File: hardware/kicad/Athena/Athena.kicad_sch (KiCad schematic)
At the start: 0 parts

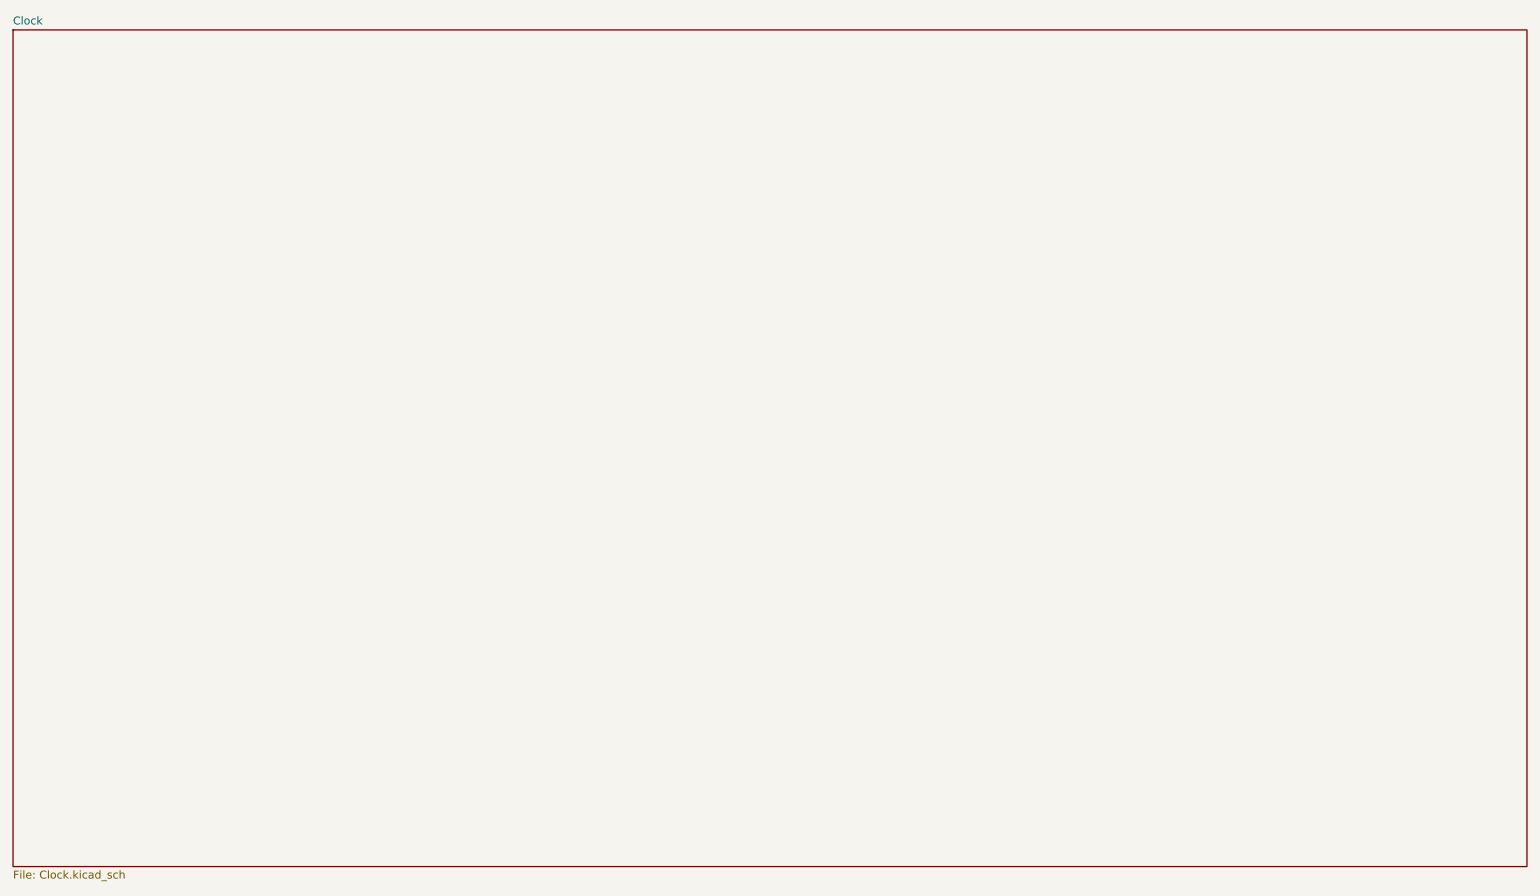
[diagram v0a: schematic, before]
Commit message: Document clock verification and initial Z80 bring-up
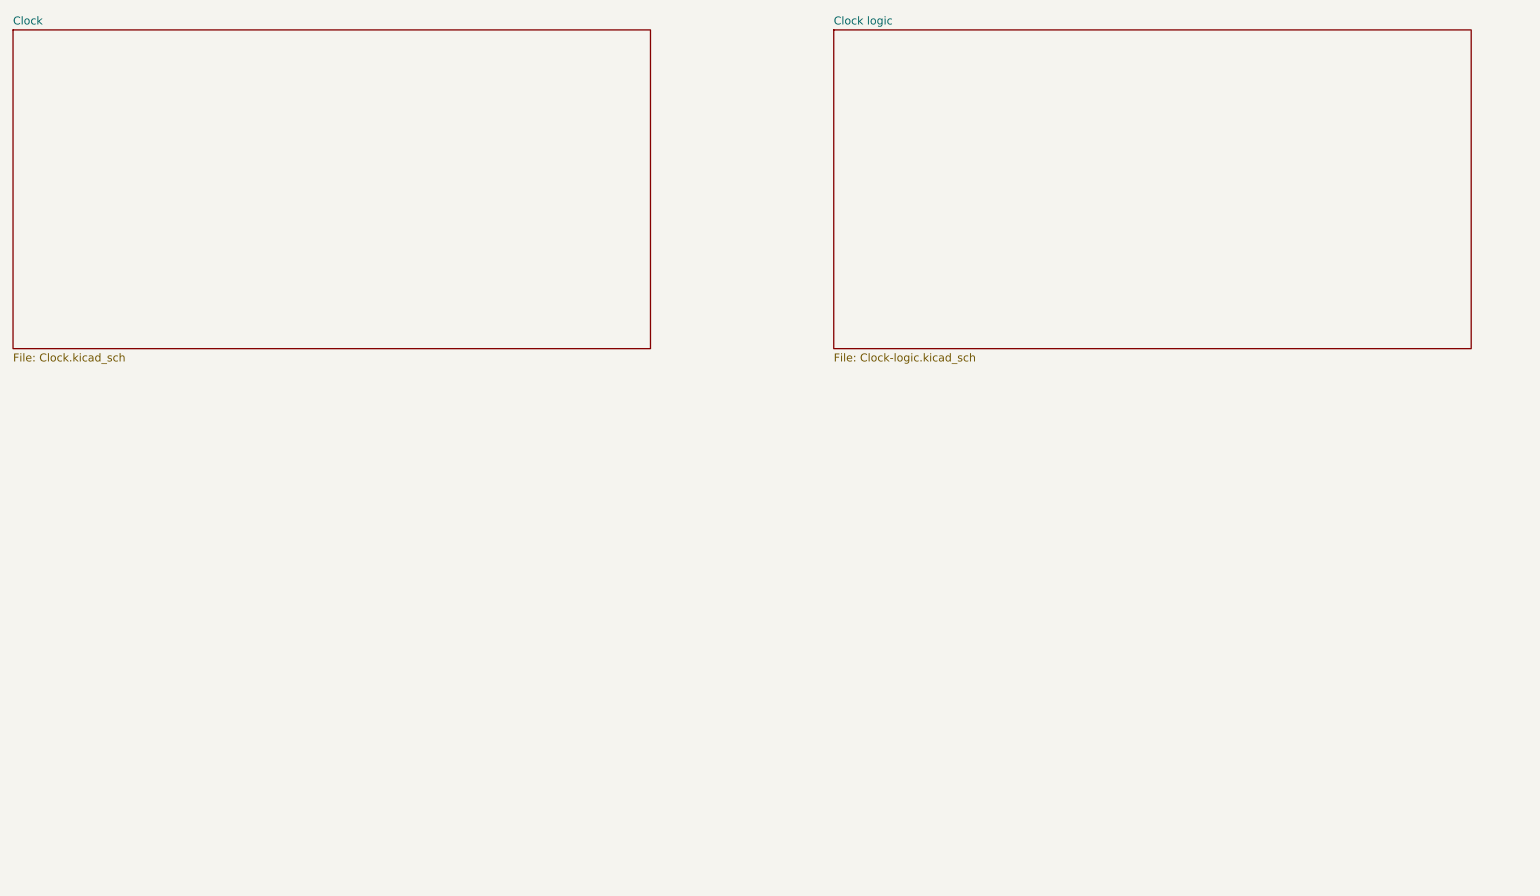
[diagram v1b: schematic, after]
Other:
- added sheet Clock logic (Clock-logic.kicad_sch)
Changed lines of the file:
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@@
 (kicad_sch
-	(version 20260306)
-	(generator "eeschema")
-	(generator_version "10.0")
-	(paper "A4")
-	(sheet
-		(at 29.21 25.4)
-		(size 241.3 133.35)
-		(exclude_from_sim no)
-		(in_bom yes)
-		(on_board yes)
-		(dnp no)
-		(fields_autoplaced yes)
-		(stroke
-			(width 0.1524)
-			(type solid)
-		)
-		(fill
-			(color 0 0 0 0)
-		)
-		(property "Sheetname" "Clock"
-			(at 29.21 24.6884 0)
-			(show_name no)
-			(do_not_autoplace no)
-			(effects
-				(font
-					(size 1.27 1.27)
-				)
-				(justify left bottom)
-			)
-		)
-		(property "Sheetfile" "Clock.kicad_sch"
-			(at 29.21 159.3346 0)
-			(show_name no)
-			(do_not_autoplace no)
-			(effects
-				(font
-					(size 1.27 1.27)
-				)
-				(justify left top)
-			)
-		)
-		(instances
-			(project "Athena"
-				(path "/9fb9234b-b300-4604-94c7-9e07849044c2"
-					(page "2")
-				)
-			)
-		)
-	)
-	(sheet_instances
-		(path "/"
-			(page "1")
-		)
-	)
-	(embedded_fonts no)
-)
+  (version 20260306)
+  (generator "eeschema")
+  (generator_version "10.0")
+  (paper "A4")
+  (sheet
+    (at 29.21 25.4)
+    (size 101.6 50.8)
+    (exclude_from_sim no)
+    (in_bom yes)
+    (on_board yes)
+    (dnp no)
+    (fields_autoplaced yes)
+    (stroke
+      (width 0.1524)
+      (type solid))
+    (fill
+      (color 0 0 0 0))
+    (property "Sheetname" "Clock"
+      (at 29.21 24.6884 0)
+      (show_name no)
+      (do_not_autoplace no)
+      (effects
+        (font
+          (size 1.27 1.27))
+        (justify left bottom)))
+    (property "Sheetfile" "Clock.kicad_sch"
+      (at 29.21 76.9116 0)
+      (show_name no)
+      (do_not_autoplace no)
+      (effects
+        (font
+          (size 1.27 1.27))
+        (justify left top)))
+    (instances
+      (project "Athena"
+        (path "/9fb9234b-b300-4604-94c7-9e07849044c2"
+          (page "2")))))
+  (sheet_instances
+    (path "/"
+      (page "1")))
+  (embedded_fonts no)
+  (sheet
+    (at 160.02 25.4)
+    (size 101.6 50.8)
+    (exclude_from_sim yes)
+    (in_bom no)
+    (on_board no)
+    (dnp no)
+    (fields_autoplaced yes)
+    (stroke
+      (width 0.1524)
+      (type solid))
+    (fill
+      (color 0 0 0 0))
+    (property "Sheetname" "Clock logic"
+      (at 160.02 24.6884 0)
+      (show_name no)
+      (do_not_autoplace no)
+      (effects
+        (font
+          (size 1.27 1.27))
+        (justify left bottom)))
+    (property "Sheetfile" "Clock-logic.kicad_sch"
+      (at 160.02 76.9116 0)
+      (show_name no)
+      (do_not_autoplace no)
+      (effects
+        (font
+          (size 1.27 1.27))
+        (justify left top)))
+    (instances
+      (project "Athena"
+        (path "/9fb9234b-b300-4604-94c7-9e07849044c2"
+          (page "3"))))))
